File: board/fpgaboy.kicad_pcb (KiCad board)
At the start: 4 copper layers, 50 x 50 mm, 88 parts, among them J1 Conn_01x12, J2 Conn_01x06, J3 Micro_SD_Card_Det, J4 Conn_01x06, P1 ILI9341, P2 CONN_01X02, P3 USB_OTG, Q1 BSS816NW, SW1 SWITCH_SPST, U1 iCE40-HX8k-BG121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

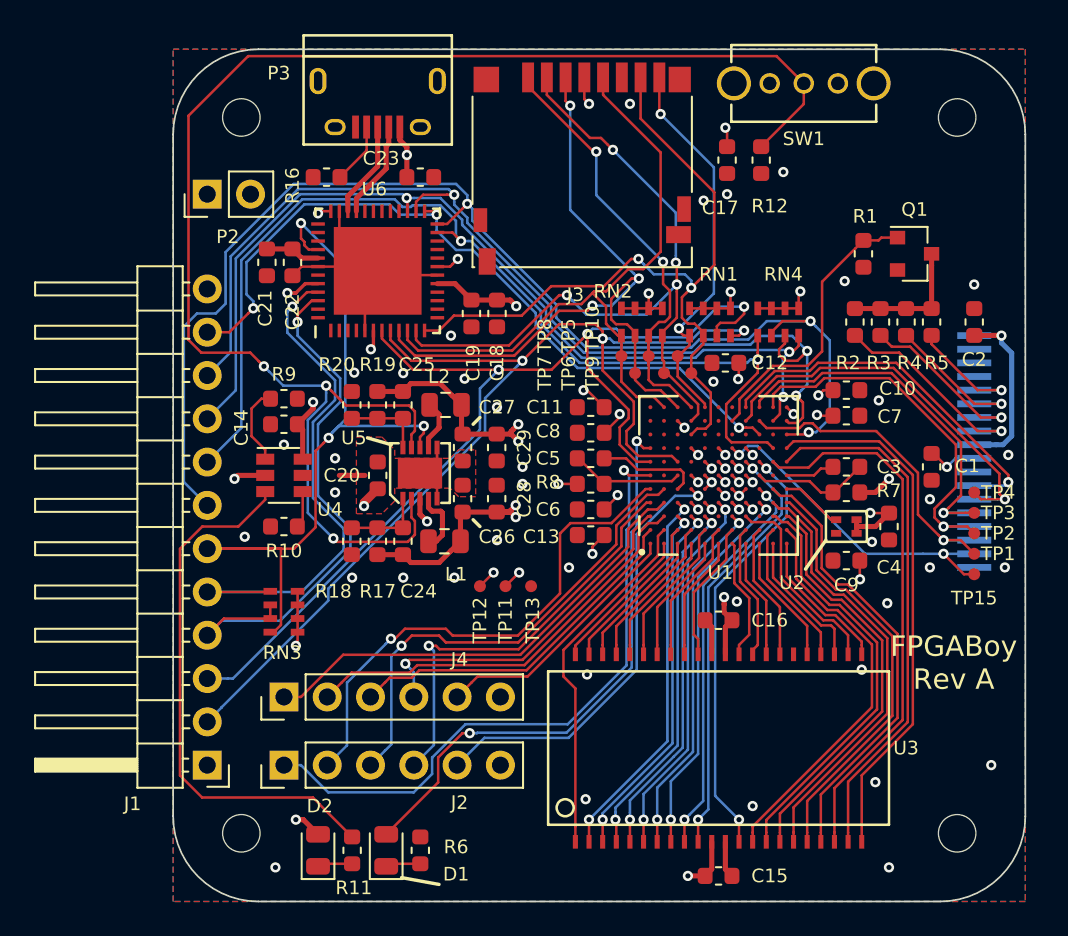
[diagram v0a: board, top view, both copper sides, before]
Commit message: Tidy up silk screen. Add some more ground stitching. Dress some traces. Add thermal thru-plane underneath SMPS
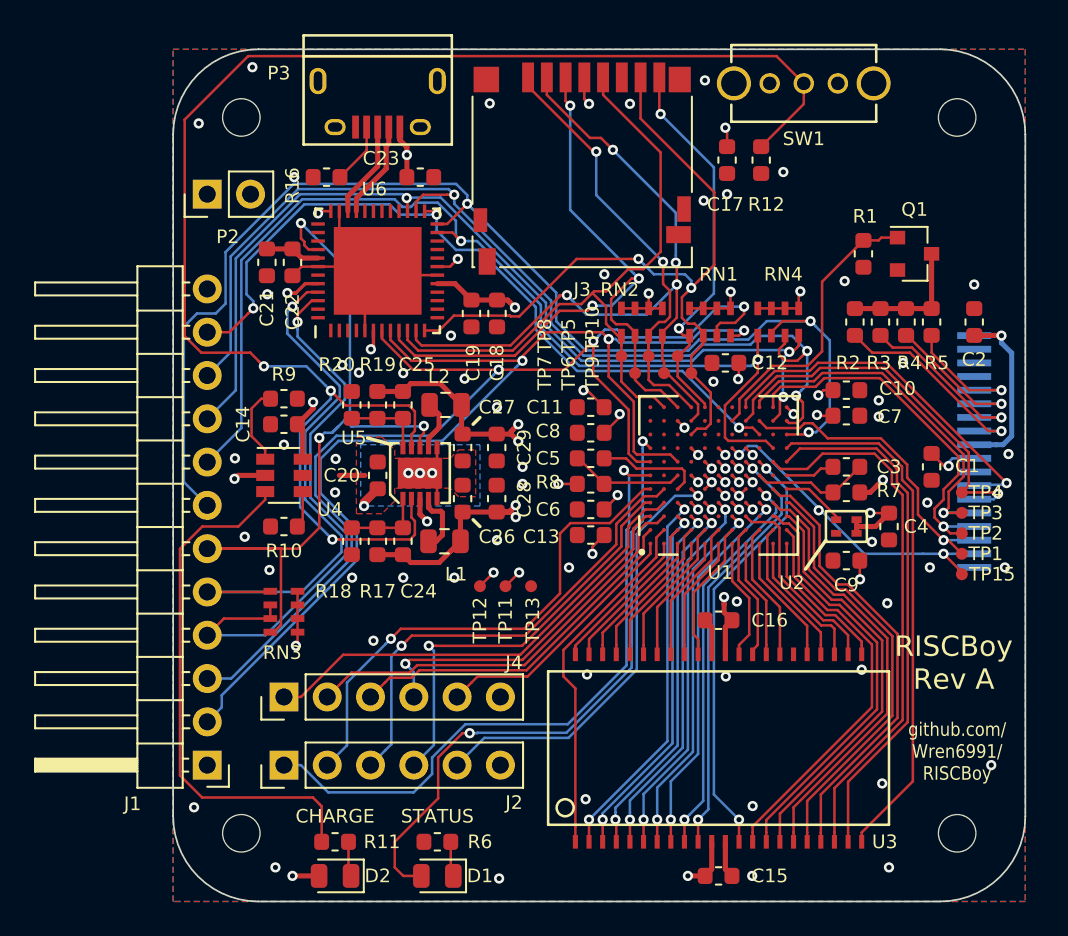
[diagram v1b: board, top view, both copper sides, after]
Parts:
- moved D1 3.35 mm to (145.5, 128.5), turned to 180 degrees
- moved D2 1.80 mm to (139.5, 128.5), turned to 180 degrees
- moved R11 1.12 mm to (139.5, 126.5), turned to 180 degrees
- moved R6 1.12 mm to (145.5, 126.5), turned to 180 degrees
- moved TP1 0.72 mm to (176.3, 109.6)
- moved TP15 0.72 mm to (176.3, 110.8)
- moved TP2 0.72 mm to (176.3, 108.4)
- moved TP3 0.72 mm to (176.3, 107.2)
- moved TP4 0.72 mm to (176.3, 106.0)
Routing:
- net /FPGA_UART_RX: track 64.0 -> 68.3 mm
- net /FPGA_UART_TX: track 63.3 -> 67.3 mm
- net /FPGA_HEARTBEAT: track 33.7 -> 37.0 mm
- net +BATT: track 147.6 -> 144.9 mm
- net /LCD_SDA: track 24.6 -> 23.1 mm
- net /LCD_D~C~: track 22.8 -> 21.9 mm
- net /LCD_CS: track 22.7 -> 21.8 mm
- net /LCD_SCL: track 19.3 -> 18.5 mm
- net /FPGA_CFG_DONE: track 60.9 -> 61.6 mm
- net /LCD_RESET: track 19.5 -> 18.8 mm
- net GNDPWR: vias 0 -> 3
- net GND: vias 47 -> 65
- added copper zone on B.Cu, net GNDPWR
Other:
- board text added: "CHARGE"
- board text added: "RISCBoy Rev A"
- board text added: "STATUS"
- board text added: "github.com/ Wren6991/ RISCBoy"
- board text removed: "FPGABoy Rev A"

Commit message: Tidy up potential ground antenna on backside plane (stitch + shorten)
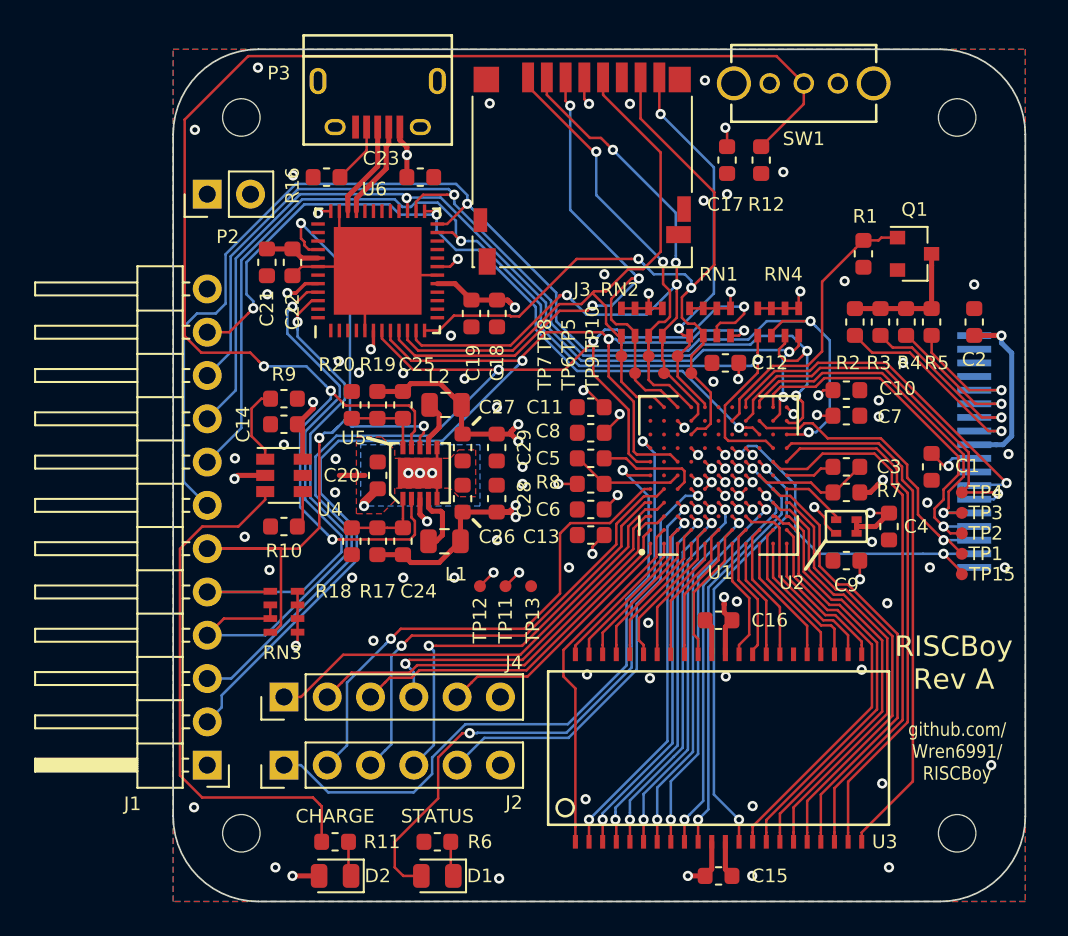
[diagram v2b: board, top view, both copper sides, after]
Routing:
- net GND: track 23.1 -> 25.2 mm, vias 65 -> 67
- net /LCD_RESET: track 18.8 -> 20.4 mm
- net /GPIO_SW0: track 37.7 -> 38.8 mm
- net /FPGA_HEARTBEAT: track 37.0 -> 37.6 mm

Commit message: Add script to generate FPGA PCF from kicad netlist. Also some tidying up of the power supply routing.
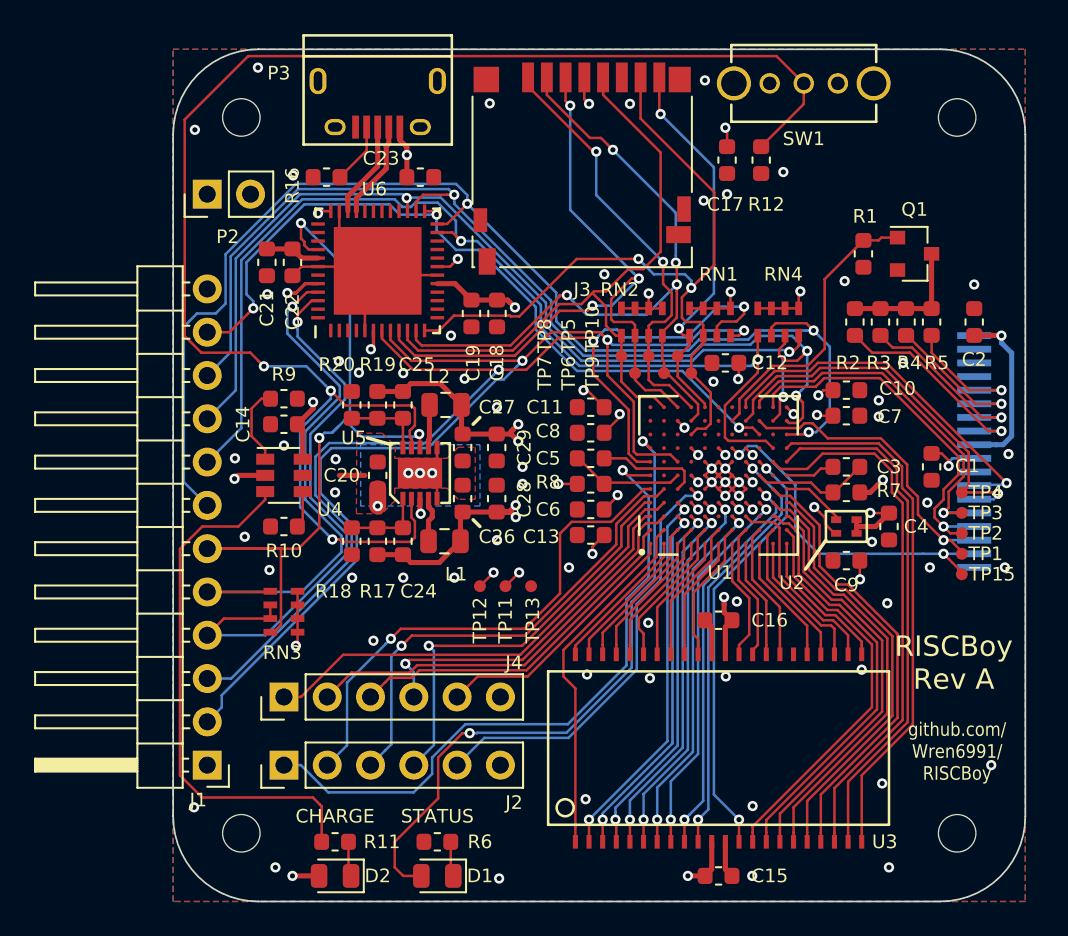
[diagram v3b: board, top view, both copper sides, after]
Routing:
- net GND: track 25.2 -> 32.6 mm, vias 67 -> 66
- net +BATT: track 144.9 -> 143.8 mm
- net Net-(L1-Pad1): track 3.74 -> 2.68 mm
- net /uC_~RST: track 45.7 -> 45.2 mm

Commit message: Correct orientation of LCD connector (oops), and add rudimentary audio to board.
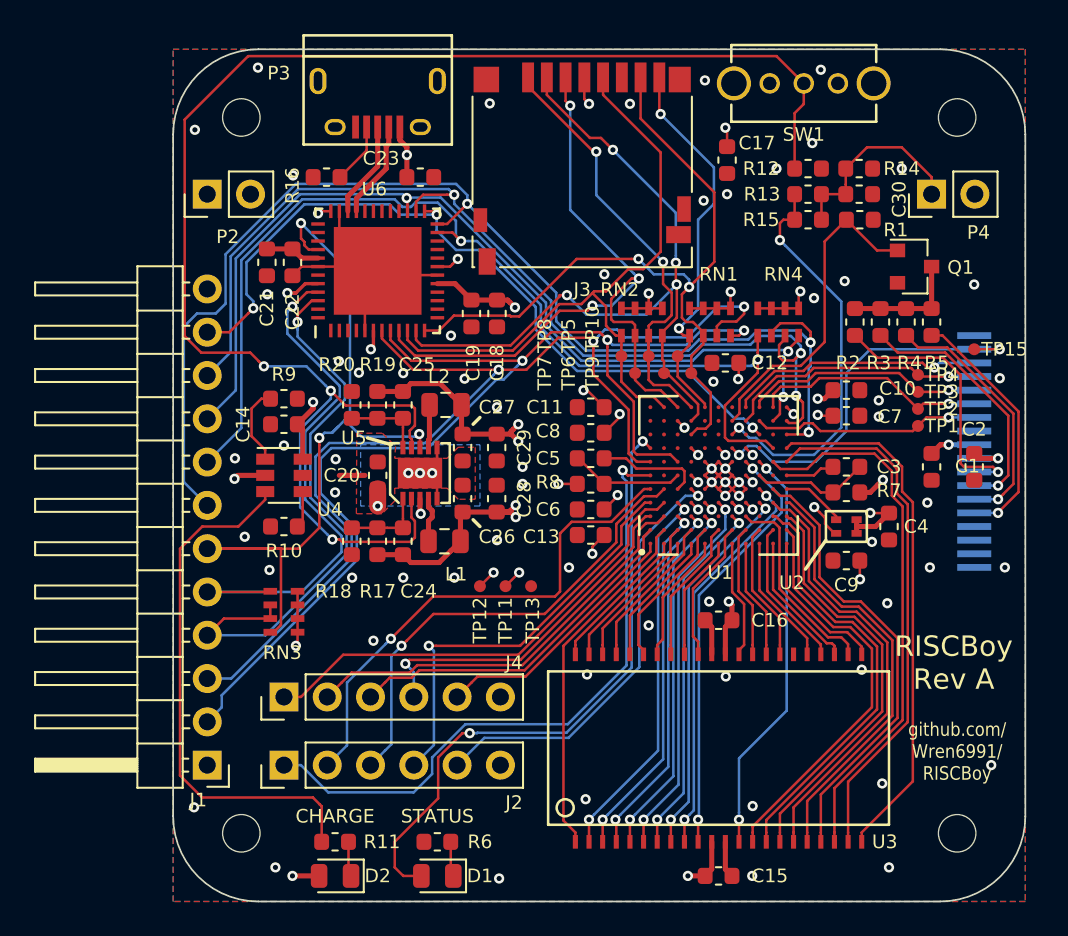
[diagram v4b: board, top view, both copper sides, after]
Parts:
- added C30: 0.1u, Capacitor_SMD:C_0603_1608Metric, F.Cu at (170.2, 88.5)
- added P4: CONN_01X02, Connector_PinHeader_2.54mm:PinHeader_1x02_P2.54mm_Vertical, F.Cu at (174.5, 88.5)
- added R13: 680, Resistor_SMD:R_0603_1608Metric, F.Cu at (167.2, 88.5)
- added R14: 220, Resistor_SMD:R_0603_1608Metric, F.Cu at (170.2, 87.0)
- added R15: 680, Resistor_SMD:R_0603_1608Metric, F.Cu at (167.2, 90.0)
- moved TP15 13.2 mm to (177.0, 97.6)
- moved C2 8.50 mm to (177.0, 104.5), turned to 270 degrees
- moved TP1 7.93 mm to (173.7, 102.1)
- moved TP2 7.74 mm to (173.7, 101.1)
- moved TP3 7.55 mm to (173.7, 100.1)
- moved TP4 7.36 mm to (173.7, 99.1)
- moved R12 2.80 mm to (167.2, 87.0), turned to 0 degrees
- moved R1 2.01 mm to (170.3, 90.0), turned to 0 degrees
- moved Q1 0.75 mm to (173.5, 92.8)
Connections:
- P1 pad 3: /LCD_SCL -> /LCD_SDO
- P1 pad 4: /LCD_D~C~ -> /LCD_SDA
- P1 pad 6: /LCD_SDA -> /LCD_D~C~
- P1 pad 7: /LCD_SDO -> /LCD_SCL
- U1 pad G9: Net-(U1-PadG9) -> /AUDIO_PWM
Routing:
- net /AUDIO_PWM: track 0.00 -> 23.8 mm, vias 0 -> 2
- net Net-(C30-Pad1): track 0.00 -> 11.7 mm
- net /LCD_D~C~: track 21.9 -> 13.8 mm
- net /LCD_SDA: track 23.1 -> 15.4 mm
- net /LCD_CS: track 21.8 -> 14.1 mm
- net Net-(P1-Pad14): track 7.62 -> 14.8 mm
- net /LCD_SDO: track 21.5 -> 15.0 mm
- net Net-(P1-Pad13): track 8.86 -> 15.0 mm
- net Net-(P1-Pad12): track 10.7 -> 16.1 mm
- net /LCD_SCL: track 18.6 -> 13.4 mm
- net Net-(P1-Pad11): track 12.5 -> 16.2 mm
- net /LCD_RESET: track 20.4 -> 22.7 mm
- net /LCD_PWM: track 17.0 -> 19.3 mm
- net /FPGA_CFG_~RST: track 72.9 -> 71.6 mm
- net /SRAM_DQ5: track 25.3 -> 24.1 mm
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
